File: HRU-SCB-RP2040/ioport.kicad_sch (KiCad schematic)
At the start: 7 parts, among them J25 Conn_01x04_Pin, J26 Conn_01x04_Pin, J27 Conn_01x04_MountingPin, J28 Conn_01x04_MountingPin, J30 Micro_SD_Card_Det_Hirose_DM3AT

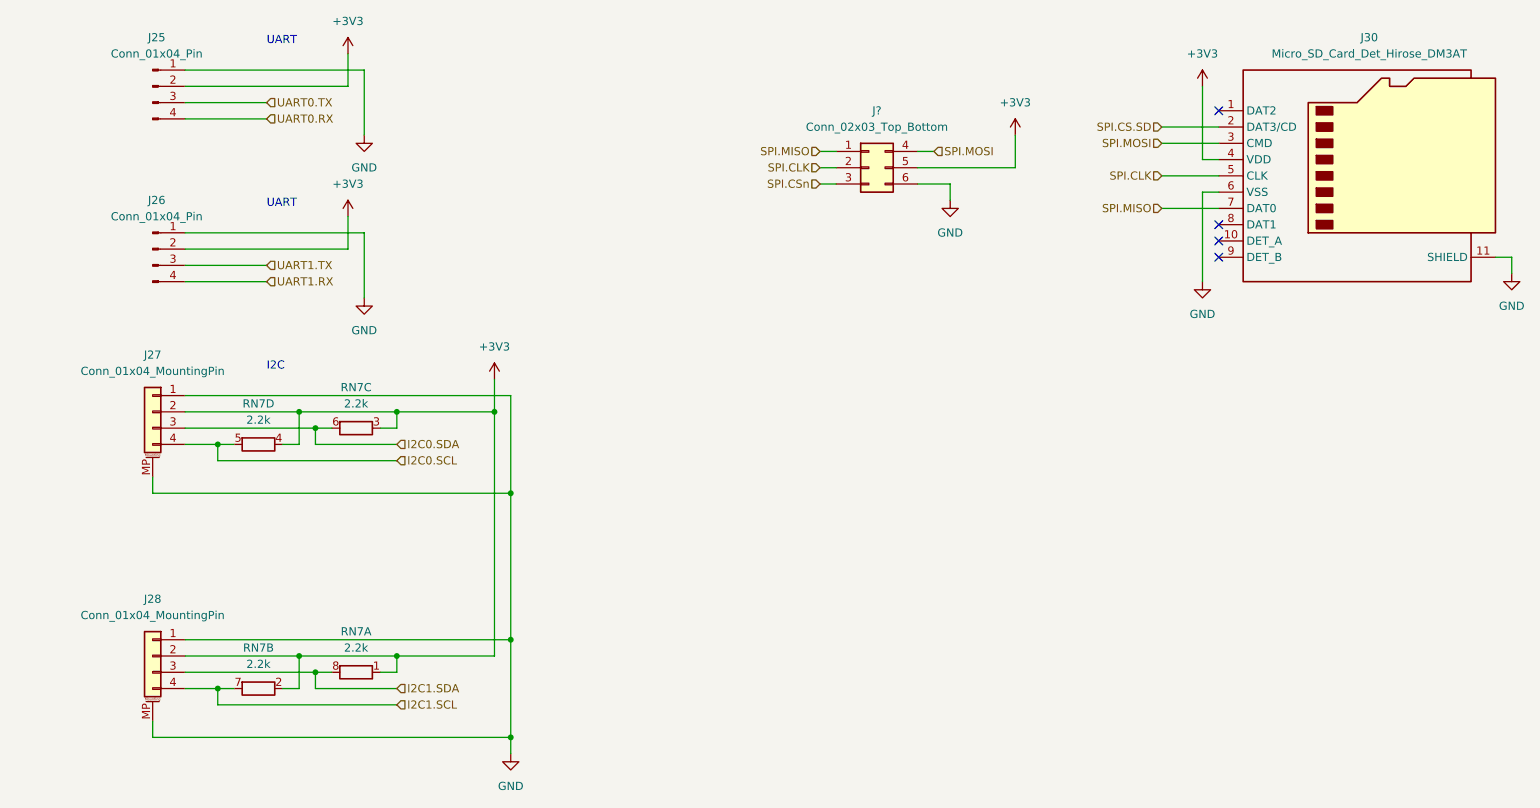
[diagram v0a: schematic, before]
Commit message: Delete PWM circuit
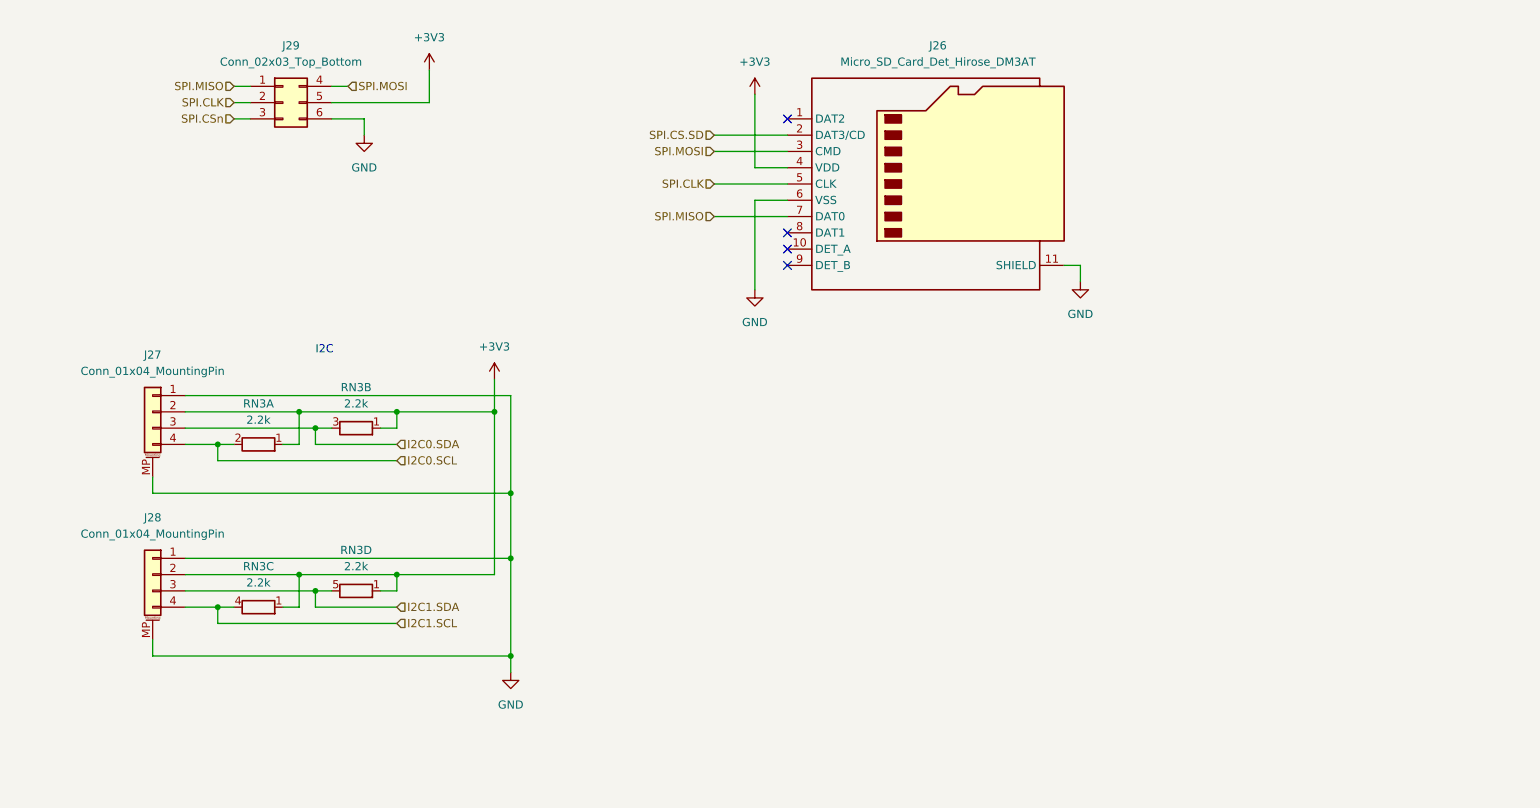
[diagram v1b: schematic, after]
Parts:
- removed J25, J26: Conn_01x04_Pin, Connector_PinHeader_2.54mm:PinHeader_1x04_P2.54mm_Vertical, symbol Connector:Conn_01x04_Pin
- removed RN7: 2.2k, Resistor_SMD:R_Array_Convex_4x1206, symbol Device:R_Pack04_Split
- added RN3: 2.2k, Resistor_THT:R_Array_SIP5, symbol Device:R_Network04_Split
- J26: renamed from J30; footprint Connector_Card:microSD_HC_Hirose_DM3D-SF -> Connector_Card:microSD_HC_Hirose_DM3AT-SF-PEJM5
- gave numbers to parts that had none: 1
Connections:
- net +3V3: now also RN3.1 (R1), RN3.1 (R1), RN3.1 (R1), RN3.1 (R1)
- net I2C0.SCL: now also RN3.2 (R1.2)
- net I2C0.SDA: now also RN3.3 (R2.2)
- net I2C1.SCL: now also RN3.4 (R3.2)
- net I2C1.SDA: now also RN3.5 (R4.2)
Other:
- note removed: "UART"
- moved on the sheet: J26, J28, J29

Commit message: Update design for hand soldering friendly
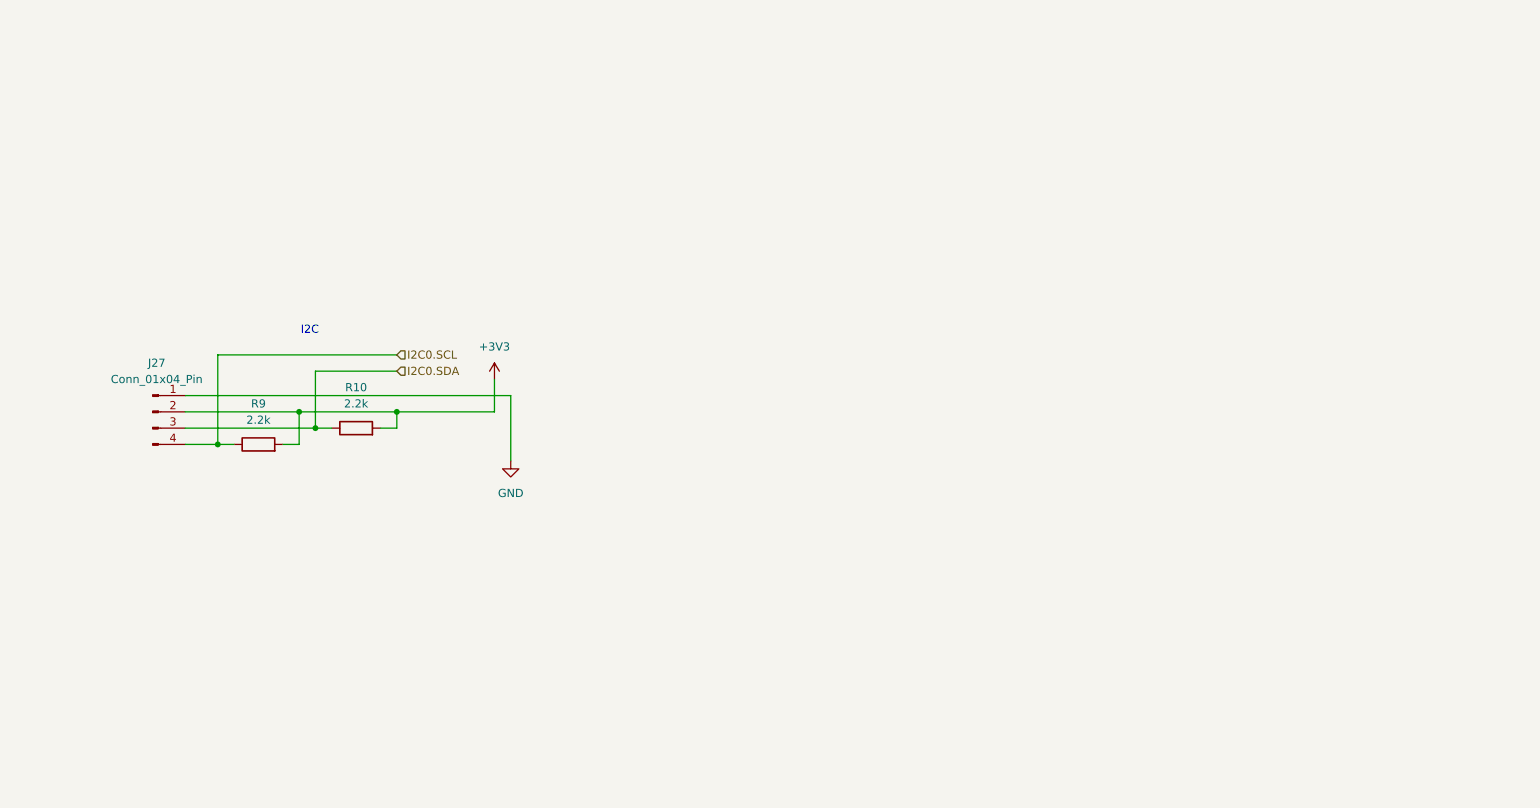
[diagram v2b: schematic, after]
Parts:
- removed J26: Micro_SD_Card_Det_Hirose_DM3AT, Connector_Card:microSD_HC_Hirose_DM3AT-SF-PEJM5, symbol Connector:Micro_SD_Card_Det_Hirose_DM3AT
- removed J27, J28: Conn_01x04_MountingPin, Connector_JST:JST_SH_SM04B-SRSS-TB_1x04-1MP_P1.00mm_Horizontal, symbol Connector_Generic_MountingPin:Conn_01x04_MountingPin
- removed J29: Conn_02x03_Top_Bottom, Connector_PinHeader_2.54mm:PinHeader_2x03_P2.54mm_Vertical, symbol Connector_Generic:Conn_02x03_Top_Bottom
- removed RN3: 2.2k, Resistor_THT:R_Array_SIP5, symbol Device:R_Network04_Split
- added J27: Conn_01x04_Pin, OPL_Connector:HW4-2.0-90D, symbol Connector:Conn_01x04_Pin
- added R10, R9: 2.2k, Resistor_THT:R_Axial_DIN0204_L3.6mm_D1.6mm_P5.08mm_Horizontal, symbol Device:R
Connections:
- net +3V3: now also J27.2 (Pin_2), R10.2, R9.2
- net GND: now also J27.1 (Pin_1)
- net I2C0.SCL: now also J27.4 (Pin_4), R9.1
- net I2C0.SDA: now also J27.3 (Pin_3), R10.1
- no-connect marks 4 -> 0

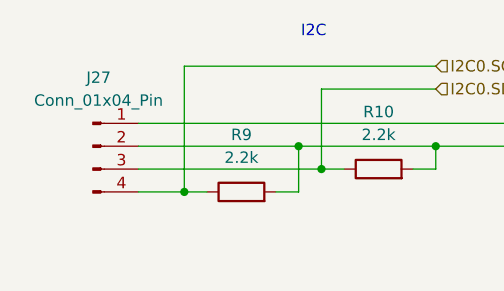
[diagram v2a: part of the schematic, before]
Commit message: Update DCDC for DIP soldering
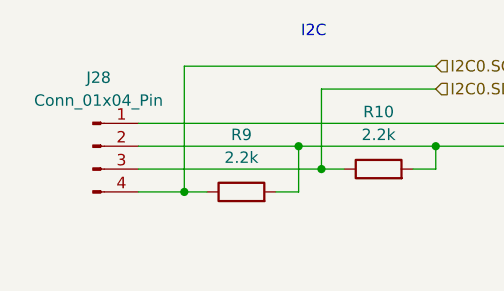
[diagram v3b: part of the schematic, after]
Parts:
- J28: renamed from J27; footprint OPL_Connector:HW4-2.0-90D -> mymod:PinHeader_1x04_P2.54mm_Vertical_SmallCourtyard
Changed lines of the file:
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@@
 		(dnp no)
 		(fields_autoplaced yes)
-		(property "Reference" "J27"
+		(property "Reference" "J28"
 			(at 46.355 83.82 0)
 			(effects
@@
 			)
 		)
-		(property "Footprint" "OPL_Connector:HW4-2.0-90D"
+		(property "Footprint" "mymod:PinHeader_1x04_P2.54mm_Vertical_SmallCourtyard"
 			(at 45.72 91.44 0)
 			(effects
@@
 			(project "HRU-SCB-RP2040"
 				(path "/22d57d1f-fa00-4148-a62a-8eb596ebbd21/e77e8245-6b3f-4da7-90e6-d027ac806a87"
-					(reference "J27")
+					(reference "J28")
 					(unit 1)
 				)

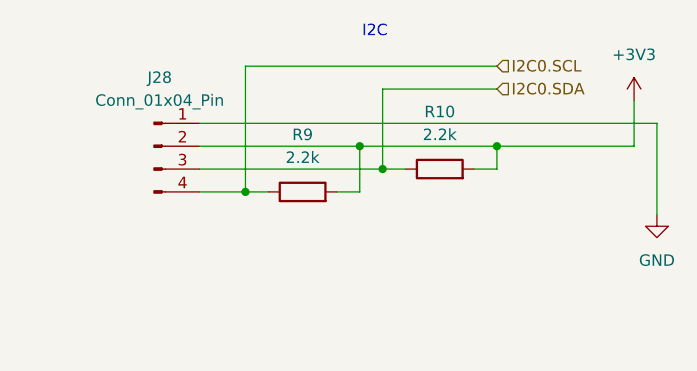
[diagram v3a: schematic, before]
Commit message: Modify footprint of the registers and regulators
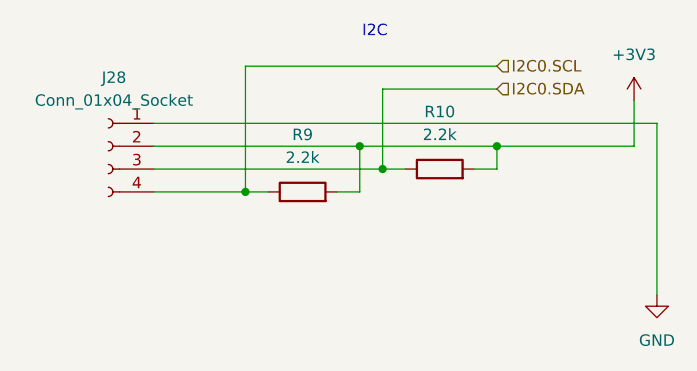
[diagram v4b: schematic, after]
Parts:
- removed J28: Conn_01x04_Pin, mymod:PinHeader_1x04_P2.54mm_Vertical_SmallCourtyard, symbol Connector:Conn_01x04_Pin
- added J28: Conn_01x04_Socket, Connector_PinHeader_2.00mm:PinHeader_1x04_P2.00mm_Vertical, symbol Connector:Conn_01x04_Socket
- R10, R9: footprint Resistor_THT:R_Axial_DIN0204_L3.6mm_D1.6mm_P5.08mm_Horizontal -> Resistor_THT:R_Axial_DIN0207_L6.3mm_D2.5mm_P7.62mm_Horizontal
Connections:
- net +3V3: now also J28.2 (Pin_2)
- net GND: now also J28.1 (Pin_1)
- net I2C0.SCL: now also J28.4 (Pin_4)
- net I2C0.SDA: now also J28.3 (Pin_3)
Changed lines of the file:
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@@
 	(wire
 		(pts
-			(xy 101.6 88.9) (xy 101.6 99.06)
+			(xy 101.6 88.9) (xy 101.6 107.95)
 		)
 		(stroke
@@
 	(wire
 		(pts
-			(xy 50.8 91.44) (xy 68.58 91.44)
+			(xy 45.72 91.44) (xy 68.58 91.44)
 		)
 		(stroke
@@
 	(wire
 		(pts
-			(xy 71.12 93.98) (xy 50.8 93.98)
+			(xy 71.12 93.98) (xy 45.72 93.98)
 		)
 		(stroke
@@
 	(wire
 		(pts
-			(xy 50.8 88.9) (xy 101.6 88.9)
+			(xy 45.72 88.9) (xy 101.6 88.9)
 		)
 		(stroke
@@
 	(wire
 		(pts
-			(xy 55.88 96.52) (xy 50.8 96.52)
+			(xy 55.88 96.52) (xy 45.72 96.52)
 		)
 		(stroke
@@
 	)
 	(symbol
+		(lib_id "Connector:Conn_01x04_Socket")
+		(at 40.64 91.44 0)
+		(mirror y)
+		(unit 1)
+		(exclude_from_sim no)
+		(in_bom yes)
+		(on_board yes)
+		(dnp no)
+		(fields_autoplaced yes)
+		(property "Reference" "J28"
+			(at 41.275 83.82 0)
+			(effects
+				(font
+					(size 1.27 1.27)
+				)
+			)
+		)
+		(property "Value" "Conn_01x04_Socket"
+			(at 41.275 86.36 0)
+			(effects
+				(font
+					(size 1.27 1.27)
+				)
+			)
+		)
+		(property "Footprint" "Connector_PinHeader_2.00mm:PinHeader_1x04_P2.00mm_Vertical"
+			(at 40.64 91.44 0)
+			(effects
+				(font
+					(size 1.27 1.27)
+				)
+				(hide yes)
+			)
+		)
+		(property "Datasheet" "~"
+			(at 40.64 91.44 0)
+			(effects
+				(font
+					(size 1.27 1.27)
+				)
+				(hide yes)
+			)
+		)
+		(property "Description" "Generic connector, single row, 01x04, script generated"
+			(at 40.64 91.44 0)
+			(effects
+				(font
+					(size 1.27 1.27)
+				)
+				(hide yes)
+			)
+		)
+		(pin "4"
+		)
+		(pin "1"
+		)
+		(pin "2"
+		)
+		(pin "3"
+		)
+		(instances
+			(project ""
+				(path "/22d57d1f-fa00-4148-a62a-8eb596ebbd21/e77e8245-6b3f-4da7-90e6-d027ac806a87"
+					(reference "J28")
+					(unit 1)
+				)
+			)
+		)
+	)
+	(symbol
 		(lib_id "Device:R")
 		(at 62.23 96.52 90)
@@
 			)
 		)
-		(property "Footprint" "Resistor_THT:R_Axial_DIN0204_L3.6mm_D1.6mm_P5.08mm_Horizontal"
+		(property "Footprint" "Resistor_THT:R_Axial_DIN0207_L6.3mm_D2.5mm_P7.62mm_Horizontal"
 			(at 62.23 98.298 90)
 			(effects
@@
 	(symbol
 		(lib_id "power:GND")
-		(at 101.6 99.06 0)
+		(at 101.6 107.95 0)
 		(unit 1)
 		(exclude_from_sim no)
@@
 		(fields_autoplaced yes)
 		(property "Reference" "#PWR017"
-			(at 101.6 105.41 0)
+			(at 101.6 114.3 0)
 			(effects
 				(font
@@
 		)
 		(property "Value" "GND"
-			(at 101.6 104.14 0)
+			(at 101.6 113.03 0)
 			(effects
 				(font
@@
 		)
 		(property "Footprint" ""
-			(at 101.6 99.06 0)
+			(at 101.6 107.95 0)
 			(effects
 				(font
@@
 		)
 		(property "Datasheet" ""
-			(at 101.6 99.06 0)
+			(at 101.6 107.95 0)
 			(effects
 				(font
@@
 		)
 		(property "Description" ""
-			(at 101.6 99.06 0)
+			(at 101.6 107.95 0)
 			(effects
 				(font
@@
 			)
 		)
-		(property "Footprint" "Resistor_THT:R_Axial_DIN0204_L3.6mm_D1.6mm_P5.08mm_Horizontal"
+		(property "Footprint" "Resistor_THT:R_Axial_DIN0207_L6.3mm_D2.5mm_P7.62mm_Horizontal"
 			(at 77.47 95.758 90)
 			(effects
@@
 					(unit 1)
 				)
-			)
-		)
-	)
-	(symbol
-		(lib_id "Connector:Conn_01x04_Pin")
-		(at 45.72 91.44 0)
-		(unit 1)
-		(exclude_from_sim no)
-		(in_bom yes)
-		(on_board yes)
-		(dnp no)
-		(fields_autoplaced yes)
-		(property "Reference" "J28"
-			(at 46.355 83.82 0)
-			(effects
-				(font
-					(size 1.27 1.27)
-				)
-			)
-		)
-		(property "Value" "Conn_01x04_Pin"
-			(at 46.355 86.36 0)
-			(effects
-				(font
-					(size 1.27 1.27)
-				)
-			)
-		)
-		(property "Footprint" "mymod:PinHeader_1x04_P2.54mm_Vertical_SmallCourtyard"
-			(at 45.72 91.44 0)
-			(effects
-				(font
-					(size 1.27 1.27)
-				)
-				(hide yes)
-			)
-		)
-		(property "Datasheet" "~"
-			(at 45.72 91.44 0)
-			(effects
-				(font
-					(size 1.27 1.27)
-				)
-				(hide yes)
-			)
-		)
-		(property "Description" "Generic connector, single row, 01x04, script generated"
-			(at 45.72 91.44 0)
-			(effects
-				(font
-					(size 1.27 1.27)
-				)
-				(hide yes)
-			)
-		)
-		(pin "3"
-		)
-		(pin "4"
-		)
-		(pin "1"
-		)
-		(pin "2"
-		)
-		(instances
-			(project "HRU-SCB-RP2040"
-				(path "/22d57d1f-fa00-4148-a62a-8eb596ebbd21/e77e8245-6b3f-4da7-90e6-d027ac806a87"
-					(reference "J28")
-					(unit 1)
-				)

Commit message: update: circuit design of HRU-SCB-RP2040
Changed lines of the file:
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@@
 (kicad_sch
-	(version 20231120)
+	(version 20250114)
 	(generator "eeschema")
-	(generator_version "8.0")
+	(generator_version "9.0")
 	(paper "A4")
-	(junction
-		(at 83.82 91.44)
-		(diameter 0)
-		(color 0 0 0 0)
-	)
-	(junction
-		(at 71.12 93.98)
-		(diameter 0)
-		(color 0 0 0 0)
-	)
-	(junction
-		(at 68.58 91.44)
-		(diameter 0)
-		(color 0 0 0 0)
-	)
-	(junction
-		(at 55.88 96.52)
-		(diameter 0)
-		(color 0 0 0 0)
-	)
-	(wire
-		(pts
-			(xy 55.88 82.55) (xy 55.88 96.52)
-		)
-		(stroke
-			(width 0)
-			(type default)
-		)
-	)
-	(wire
-		(pts
-			(xy 66.04 96.52) (xy 68.58 96.52)
-		)
-		(stroke
-			(width 0)
-			(type default)
-		)
-	)
-	(wire
-		(pts
-			(xy 71.12 85.09) (xy 71.12 93.98)
-		)
-		(stroke
-			(width 0)
-			(type default)
-		)
-	)
-	(wire
-		(pts
-			(xy 99.06 91.44) (xy 99.06 86.36)
-		)
-		(stroke
-			(width 0)
-			(type default)
-		)
-	)
-	(wire
-		(pts
-			(xy 101.6 88.9) (xy 101.6 107.95)
-		)
-		(stroke
-			(width 0)
-			(type default)
-		)
-	)
-	(wire
-		(pts
-			(xy 83.82 91.44) (xy 99.06 91.44)
-		)
-		(stroke
-			(width 0)
-			(type default)
-		)
-	)
-	(wire
-		(pts
-			(xy 45.72 91.44) (xy 68.58 91.44)
-		)
-		(stroke
-			(width 0)
-			(type default)
-		)
-	)
-	(wire
-		(pts
-			(xy 55.88 82.55) (xy 83.82 82.55)
-		)
-		(stroke
-			(width 0)
-			(type default)
-		)
-	)
-	(wire
-		(pts
-			(xy 81.28 93.98) (xy 83.82 93.98)
-		)
-		(stroke
-			(width 0)
-			(type default)
-		)
-	)
-	(wire
-		(pts
-			(xy 68.58 96.52) (xy 68.58 91.44)
-		)
-		(stroke
-			(width 0)
-			(type default)
-		)
-	)
-	(wire
-		(pts
-			(xy 68.58 91.44) (xy 83.82 91.44)
-		)
-		(stroke
-			(width 0)
-			(type default)
-		)
-	)
-	(wire
-		(pts
-			(xy 71.12 85.09) (xy 83.82 85.09)
-		)
-		(stroke
-			(width 0)
-			(type default)
-		)
-	)
-	(wire
-		(pts
-			(xy 71.12 93.98) (xy 45.72 93.98)
-		)
-		(stroke
-			(width 0)
-			(type default)
-		)
-	)
-	(wire
-		(pts
-			(xy 83.82 93.98) (xy 83.82 91.44)
-		)
-		(stroke
-			(width 0)
-			(type default)
-		)
-	)
-	(wire
-		(pts
-			(xy 71.12 93.98) (xy 73.66 93.98)
-		)
-		(stroke
-			(width 0)
-			(type default)
-		)
-	)
-	(wire
-		(pts
-			(xy 45.72 88.9) (xy 101.6 88.9)
-		)
-		(stroke
-			(width 0)
-			(type default)
-		)
-	)
-	(wire
-		(pts
-			(xy 55.88 96.52) (xy 58.42 96.52)
-		)
-		(stroke
-			(width 0)
-			(type default)
-		)
-	)
-	(wire
-		(pts
-			(xy 55.88 96.52) (xy 45.72 96.52)
-		)
-		(stroke
-			(width 0)
-			(type default)
-		)
-	)
 	(text "I2C"
 		(exclude_from_sim no)
@@
 		)
 	)
+	(junction
+		(at 83.82 91.44)
+		(diameter 0)
+		(color 0 0 0 0)
+	)
+	(junction
+		(at 71.12 93.98)
+		(diameter 0)
+		(color 0 0 0 0)
+	)
+	(junction
+		(at 68.58 91.44)
+		(diameter 0)
+		(color 0 0 0 0)
+	)
+	(junction
+		(at 55.88 96.52)
+		(diameter 0)
+		(color 0 0 0 0)
+	)
+	(wire
+		(pts
+			(xy 55.88 82.55) (xy 55.88 96.52)
+		)
+		(stroke
+			(width 0)
+			(type default)
+		)
+	)
+	(wire
+		(pts
+			(xy 66.04 96.52) (xy 68.58 96.52)
+		)
+		(stroke
+			(width 0)
+			(type default)
+		)
+	)
+	(wire
+		(pts
+			(xy 71.12 85.09) (xy 71.12 93.98)
+		)
+		(stroke
+			(width 0)
+			(type default)
+		)
+	)
+	(wire
+		(pts
+			(xy 99.06 91.44) (xy 99.06 86.36)
+		)
+		(stroke
+			(width 0)
+			(type default)
+		)
+	)
+	(wire
+		(pts
+			(xy 101.6 88.9) (xy 101.6 107.95)
+		)
+		(stroke
+			(width 0)
+			(type default)
+		)
+	)
+	(wire
+		(pts
+			(xy 83.82 91.44) (xy 99.06 91.44)
+		)
+		(stroke
+			(width 0)
+			(type default)
+		)
+	)
+	(wire
+		(pts
+			(xy 45.72 91.44) (xy 68.58 91.44)
+		)
+		(stroke
+			(width 0)
+			(type default)
+		)
+	)
+	(wire
+		(pts
+			(xy 55.88 82.55) (xy 83.82 82.55)
+		)
+		(stroke
+			(width 0)
+			(type default)
+		)
+	)
+	(wire
+		(pts
+			(xy 81.28 93.98) (xy 83.82 93.98)
+		)
+		(stroke
+			(width 0)
+			(type default)
+		)
+	)
+	(wire
+		(pts
+			(xy 68.58 96.52) (xy 68.58 91.44)
+		)
+		(stroke
+			(width 0)
+			(type default)
+		)
+	)
+	(wire
+		(pts
+			(xy 68.58 91.44) (xy 83.82 91.44)
+		)
+		(stroke
+			(width 0)
+			(type default)
+		)
+	)
+	(wire
+		(pts
+			(xy 71.12 85.09) (xy 83.82 85.09)
+		)
+		(stroke
+			(width 0)
+			(type default)
+		)
+	)
+	(wire
+		(pts
+			(xy 71.12 93.98) (xy 45.72 93.98)
+		)
+		(stroke
+			(width 0)
+			(type default)
+		)
+	)
+	(wire
+		(pts
+			(xy 83.82 93.98) (xy 83.82 91.44)
+		)
+		(stroke
+			(width 0)
+			(type default)
+		)
+	)
+	(wire
+		(pts
+			(xy 71.12 93.98) (xy 73.66 93.98)
+		)
+		(stroke
+			(width 0)
+			(type default)
+		)
+	)
+	(wire
+		(pts
+			(xy 45.72 88.9) (xy 101.6 88.9)
+		)
+		(stroke
+			(width 0)
+			(type default)
+		)
+	)
+	(wire
+		(pts
+			(xy 55.88 96.52) (xy 58.42 96.52)
+		)
+		(stroke
+			(width 0)
+			(type default)
+		)
+	)
+	(wire
+		(pts
+			(xy 55.88 96.52) (xy 45.72 96.52)
+		)
+		(stroke
+			(width 0)
+			(type default)
+		)
+	)
 	(hierarchical_label "I2C0.SDA"
 		(shape input)
 		(at 83.82 85.09 0)
-		(fields_autoplaced yes)
 		(effects
 			(font
@@
 		(shape input)
 		(at 83.82 82.55 0)
-		(fields_autoplaced yes)
 		(effects
 			(font
